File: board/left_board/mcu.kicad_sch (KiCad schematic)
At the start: 2 parts, among them J401 UART, U401 STM32G0B0CETx

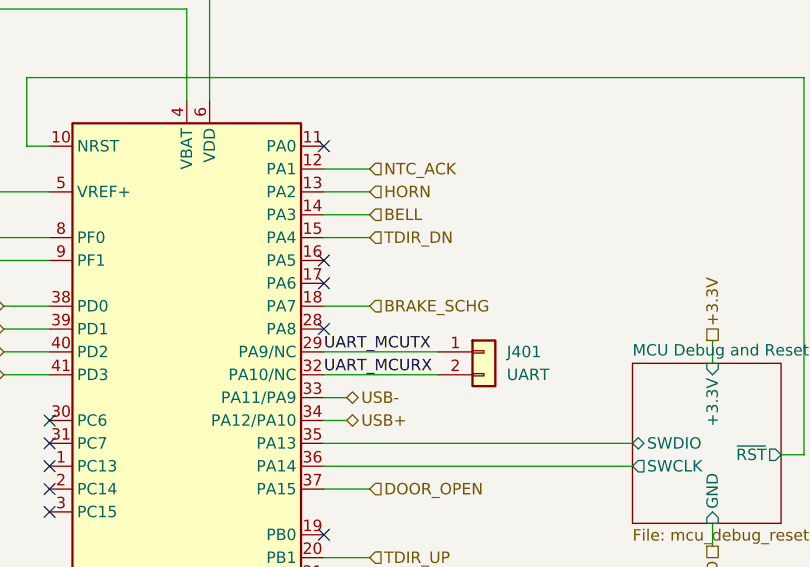
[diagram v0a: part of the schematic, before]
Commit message: add support for pedal
the pedal is mostly envisioned as a secondary dead man's switch input, but
to enable flexible usage, it is wired up to the µC's ADC and supplies
12-bit values for the X axis

things will be set up to cooperate with a Brother-compatible sewing machine
pedal because that's what I have lying around -- those that connect using a
3.5mm TS phone connector, nothing even close to mains voltage
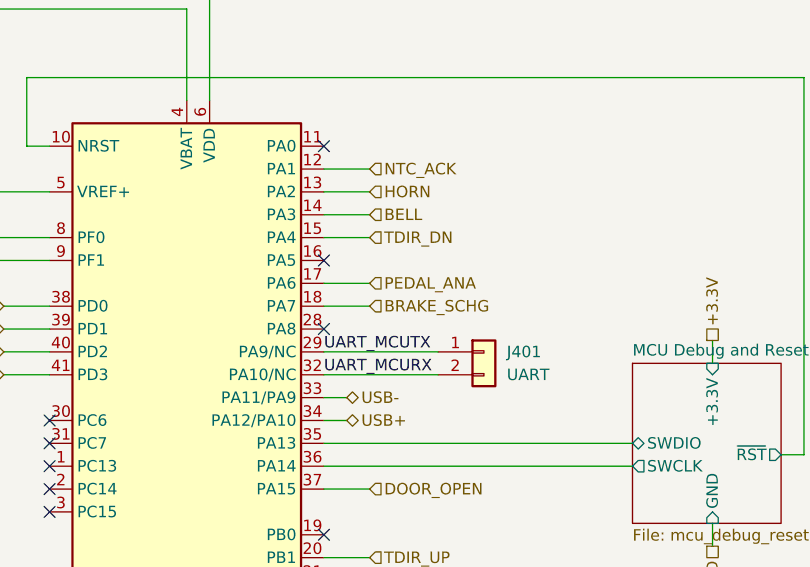
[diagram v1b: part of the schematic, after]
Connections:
- net PEDAL_ANA: now reaches U401.17 (PA6)
- no-connect marks 12 -> 11
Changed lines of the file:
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@@
-	)
-	(no_connect
-		(at 146.05 59.69)
 	)
 	(no_connect
@@
 		(pts
 			(xy 105.41 49.53) (xy 105.41 31.75)
+		)
+		(stroke
+			(width 0)
+			(type default)
+		)
+	)
+	(wire
+		(pts
+			(xy 146.05 59.69) (xy 151.13 59.69)
 		)
 		(stroke
@@
 		)
 	)
+	(hierarchical_label "PEDAL_ANA"
+		(shape input)
+		(at 151.13 59.69 0)
+		(fields_autoplaced yes)
+		(effects
+			(font
+				(size 1.27 1.27)
+			)
+			(justify left)
+		)
+	)
